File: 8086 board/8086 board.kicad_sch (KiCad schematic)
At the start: 55 parts, among them J1 USB, U1 P8086-2, U2 74HC32

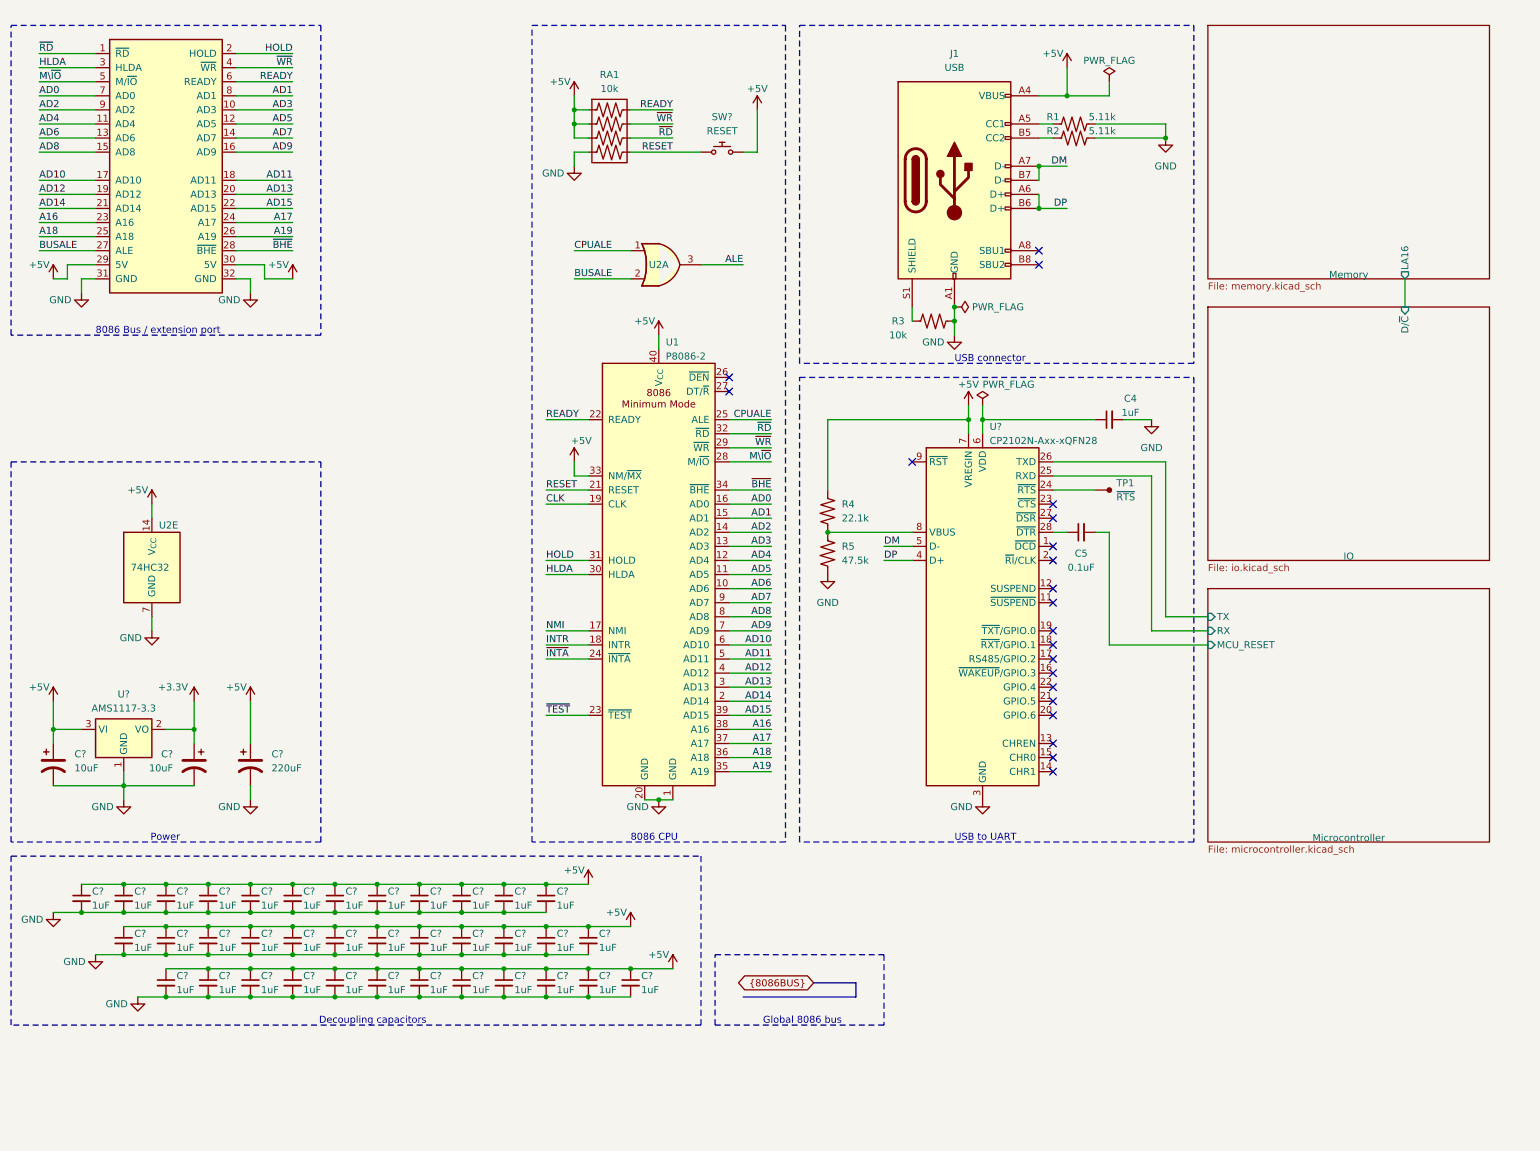
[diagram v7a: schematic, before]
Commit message: PCB: more layout work. some schematic changes.
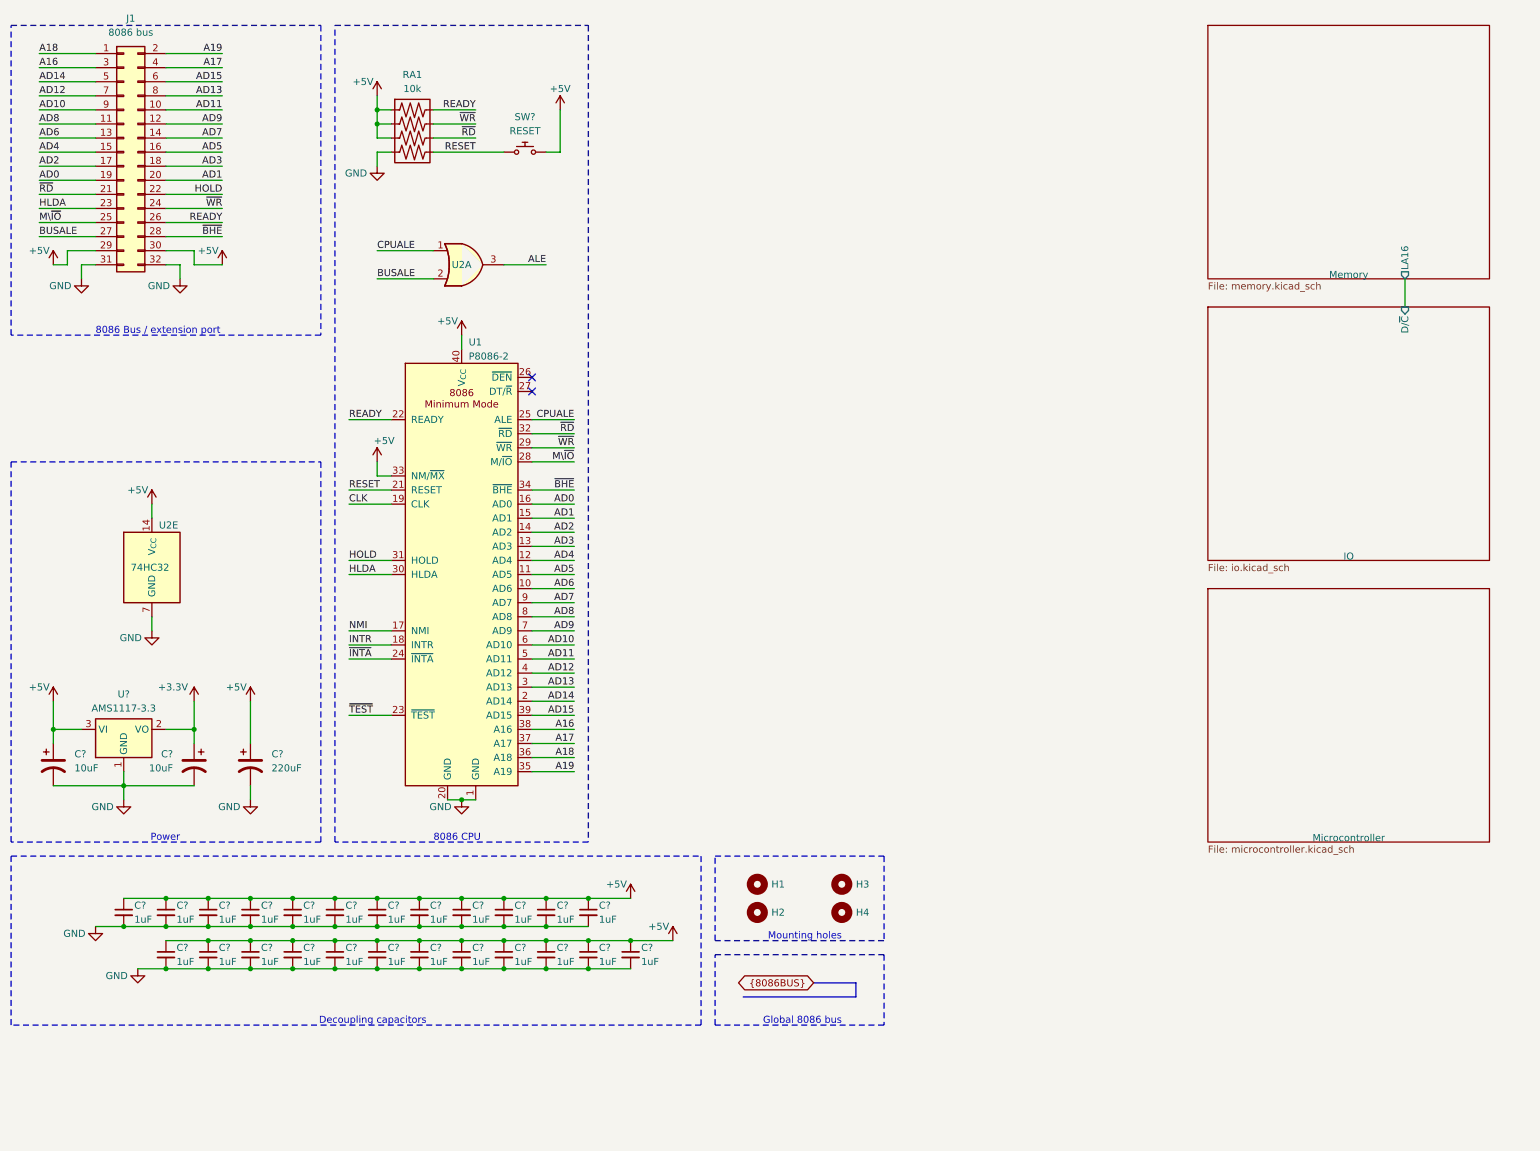
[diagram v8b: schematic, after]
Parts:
- removed BUS2: ~, Connector_PinHeader_2.54mm:PinHeader_2x16_P2.54mm_Vertical, symbol 8086PC:8086PC_BUS_REDUCED
- removed C4, C? (x12): 1uF, Capacitor_SMD:C_0603_1608Metric_Pad1.08x0.95mm_HandSolder, symbol Device:C_Small
- removed C5: 0.1uF, Capacitor_SMD:C_0603_1608Metric_Pad1.08x0.95mm_HandSolder, symbol Device:C_Small
- removed J1: USB, symbol Connector:USB_C_Receptacle_USB2.0
- removed R1, R2: 5.11k, Resistor_SMD:R_0603_1608Metric_Pad0.98x0.95mm_HandSolder, symbol 8086PC:R
- removed R3: 10k, Resistor_SMD:R_0603_1608Metric_Pad0.98x0.95mm_HandSolder, symbol 8086PC:R
- removed R4: 22.1k, Resistor_SMD:R_0603_1608Metric_Pad0.98x0.95mm_HandSolder, symbol 8086PC:R
- removed R5: 47.5k, Resistor_SMD:R_0603_1608Metric_Pad0.98x0.95mm_HandSolder, symbol 8086PC:R
- removed TP1: ~{RTS}, TestPoint:TestPoint_Pad_1.5x1.5mm, symbol 8086PC:TestPoint
- removed U?: CP2102N-Axx-xQFN28, Package_DFN_QFN:QFN-28-1EP_5x5mm_P0.5mm_EP3.35x3.35mm, symbol Interface_USB:CP2102N-Axx-xQFN28
- added H1, H2, H3, H4: ~, MountingHole:MountingHole_3.2mm_M3, symbol Mechanical:MountingHole
- added J1: 8086 bus, Connector_PinHeader_2.54mm:PinHeader_2x16_P2.54mm_Vertical, symbol Connector_Generic:Conn_02x16_Odd_Even
- SW?: footprint 8086PC:SW_Push_1P1T_NO_6x6mm_H9.5mm -> 8086PC:SW_Push_6x6x5mm
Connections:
- net +5V: now also J1.29 (Pin_29), J1.30 (Pin_30)
- net A16: now also J1.3 (Pin_3)
- net A17: now also J1.4 (Pin_4)
- net A18: now also J1.1 (Pin_1)
- net A19: now also J1.2 (Pin_2)
- net AD0: now also J1.19 (Pin_19)
- net AD1: now also J1.20 (Pin_20)
- net AD10: now also J1.9 (Pin_9)
- net AD11: now also J1.10 (Pin_10)
- net AD12: now also J1.7 (Pin_7)
- net AD13: now also J1.8 (Pin_8)
- net AD14: now also J1.5 (Pin_5)
- net AD15: now also J1.6 (Pin_6)
- net AD2: now also J1.17 (Pin_17)
- net AD3: now also J1.18 (Pin_18)
- net AD4: now also J1.15 (Pin_15)
- net AD5: now also J1.16 (Pin_16)
- net AD6: now also J1.13 (Pin_13)
- net AD7: now also J1.14 (Pin_14)
- net AD8: now also J1.11 (Pin_11)
- net AD9: now also J1.12 (Pin_12)
- net BUSALE: now also J1.27 (Pin_27)
- net GND: now also J1.31 (Pin_31), J1.32 (Pin_32)
- net HLDA: now also J1.23 (Pin_23)
- net HOLD: now also J1.22 (Pin_22)
- net M\~{IO}: now also J1.25 (Pin_25)
- net READY: now also J1.26 (Pin_26)
- net ~{BHE}: now also J1.28 (Pin_28)
- net ~{RD}: now also J1.21 (Pin_21)
- net ~{WR}: now also J1.24 (Pin_24)
- no-connect marks 21 -> 2
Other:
- sheet Microcontroller ports: added none; removed MCU_RESET, RX, TX
- note added: "Mounting holes"
- note removed: "USB connector"
- note removed: "USB to UART"
- moved on the sheet: C?, RA1, SW?, U1, U2A
